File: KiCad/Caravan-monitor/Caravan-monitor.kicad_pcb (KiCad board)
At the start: 2 copper layers, 102.5 x 80 mm, 62 parts, among them IC1 TPS54302DDCR, IC3 INA500CIDBVR, J1 Conn_ARM_JTAG_SWD_20, J2 8-28V input, J3 Outdoor temp, J4 Coolant temp, J5 Water tank 1, J6 Water tank 2, Q1 2N7002, SW2 SW_USER, SW3 SW_DPDT_x2, U1 NHD-C0220BIZ, U2 STM32L010C6Tx

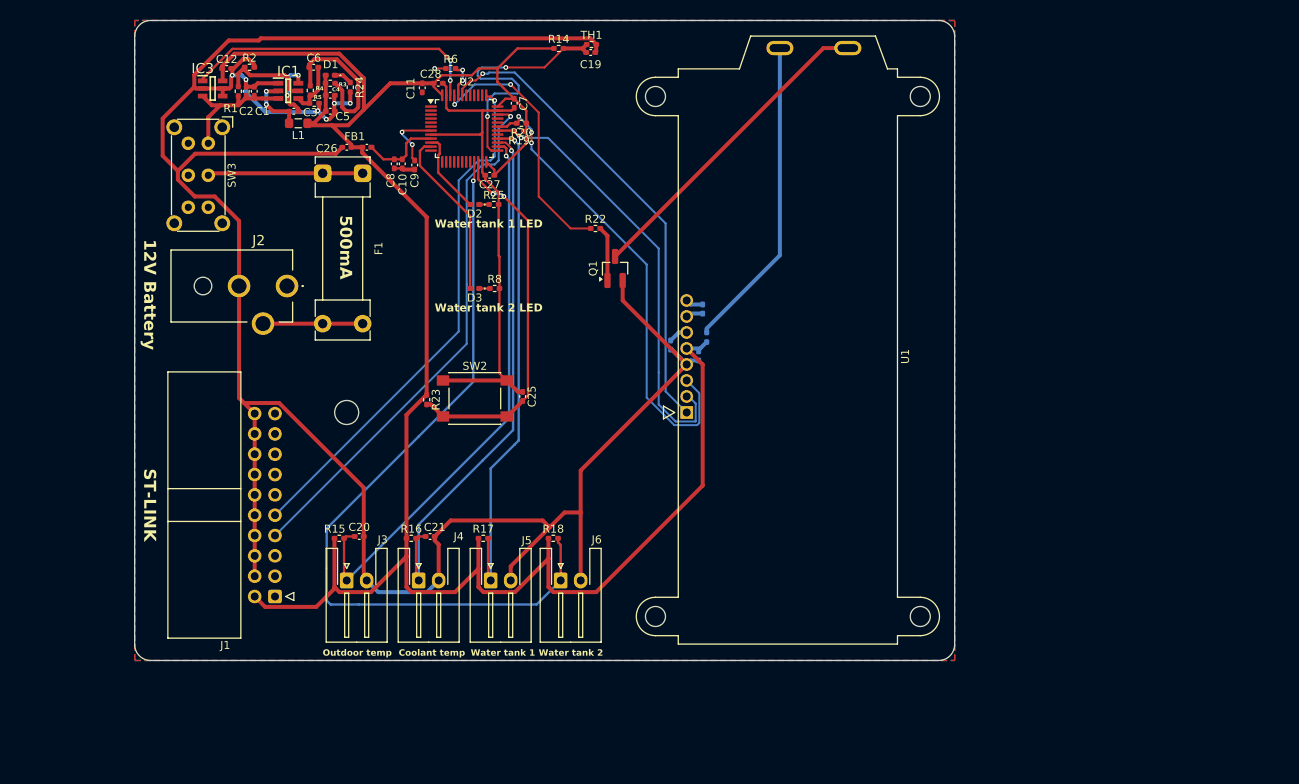
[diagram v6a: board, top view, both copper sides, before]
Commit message: 12V to 3.3V converter done
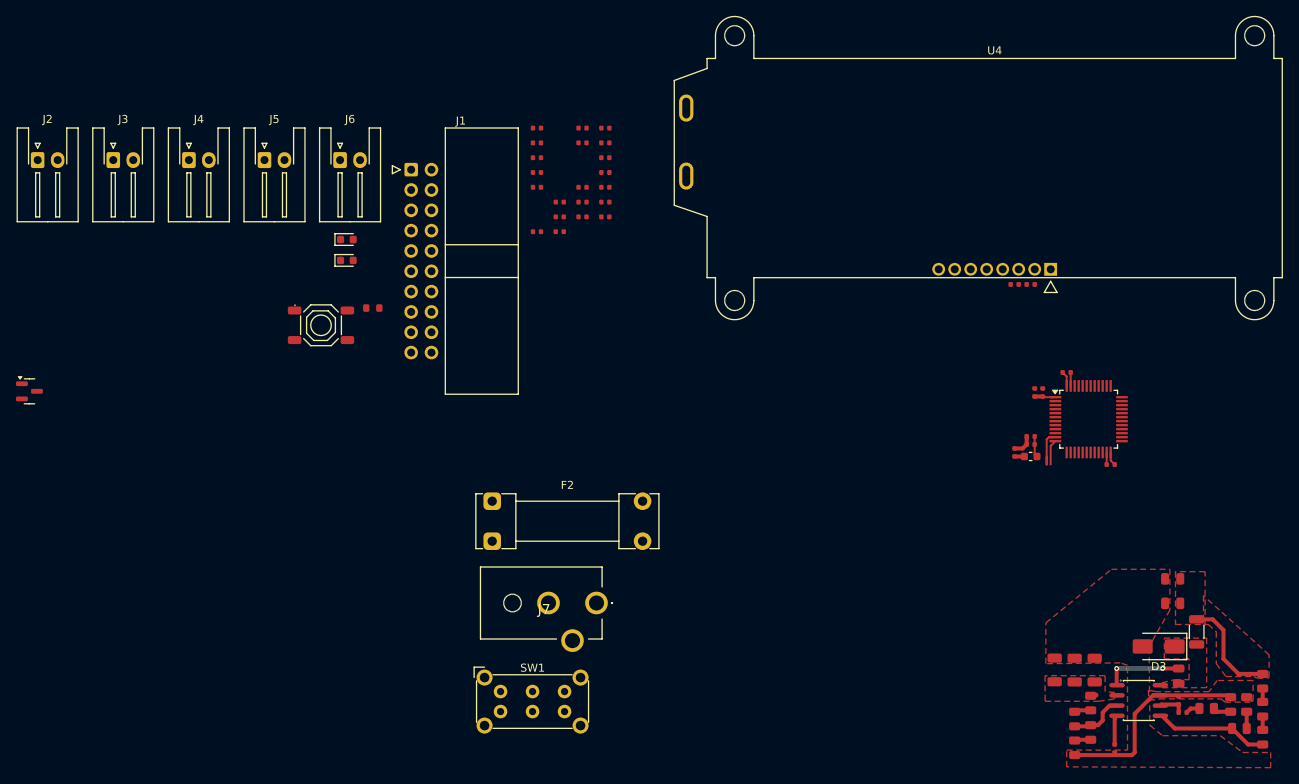
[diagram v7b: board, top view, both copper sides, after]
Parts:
- removed C19, C20, C22, C25, C27, C28: 100n, Capacitor_SMD:C_0402_1005Metric_Pad0.74x0.62mm_HandSolder
- removed C23: 0.47µ, Capacitor_SMD:C_0402_1005Metric_Pad0.74x0.62mm_HandSolder
- removed C26: 1µ, Capacitor_SMD:C_0402_1005Metric_Pad0.74x0.62mm_HandSolder
- removed D1: Power LED, LED_SMD:LED_0402_1005Metric_Pad0.77x0.64mm_HandSolder
- removed F1: 500mA, Fuse:Fuseholder_Clip-5x20mm_Littelfuse_111_Lateral_P18.80x5.00mm_D1.17mm_Horizontal
- removed G***: LOGO, LOGO
- removed IC1: TPS54302DDCR, SamacSys_Parts:SOT95P280X110-6N
- removed IC3: INA500CIDBVR, SamacSys_Parts:SOT95P280X145-6N
- removed L1: 6.8µ, Inductor_SMD:L_0805_2012Metric_Pad1.05x1.20mm_HandSolder
- removed R14: 47k, Resistor_SMD:R_0402_1005Metric_Pad0.72x0.64mm_HandSolder
- removed R17, R23: 10k, Resistor_SMD:R_0402_1005Metric_Pad0.72x0.64mm_HandSolder
- removed R20: 4.7k, Resistor_SMD:R_0402_1005Metric_Pad0.72x0.64mm_HandSolder
- removed R21: 10R, Resistor_SMD:R_0402_1005Metric_Pad0.72x0.64mm_HandSolder
- removed R22, R24, R25: 1k, Resistor_SMD:R_0402_1005Metric_Pad0.72x0.64mm_HandSolder
- removed SW2: SW_USER, Button_Switch_SMD:SW_SPST_PTS645
- removed SW3: SW_DPDT_x2, Button_Switch_THT:SW_E-Switch_EG2219_DPDT_Angled
- removed TH1: Thermistor_NTC, Resistor_SMD:R_0402_1005Metric_Pad0.72x0.64mm_HandSolder
- removed U1: NHD-C0220BIZ, Display:NHD-C0220BiZ
- added C13: 100nF, PCM_JLCPCB:C_0402, F.Cu at (147.5, 88.0)
- added C14: 10nF, PCM_JLCPCB:C_0402, F.Cu at (146.0, 93.5)
- added C15: 100nF, PCM_JLCPCB:C_0402, F.Cu at (87.1, 64.2)
- added C16: 100nF, PCM_JLCPCB:C_0402, F.Cu at (87.1, 66.0)
- added C17: 4.7uF, PCM_JLCPCB:C_1206, F.Cu at (151.5, 122.7)
- added C18: 10nF, PCM_JLCPCB:C_1206, F.Cu at (149.0, 122.7)
- added C30: 1nF, PCM_JLCPCB:C_0402, F.Cu at (165.0, 128.0)
- added C31: 47pF, PCM_JLCPCB:C_0402, F.Cu at (164.5, 126.5)
- added C32: 100nF, PCM_JLCPCB:C_0805, F.Cu at (164.5, 123.5)
- added C33: 47uF, PCM_JLCPCB:C_0805, F.Cu at (163.8, 114.3)
- added C34: 47uF, PCM_JLCPCB:C_0805, F.Cu at (163.8, 111.3)
- added D5: Red, PCM_JLCPCB:D_0603, F.Cu at (60.5, 71.5)
- added F2: 500mA, Fuse:Fuseholder_Clip-5x20mm_Littelfuse_111_Lateral_P18.80x5.00mm_D1.17mm_Horizontal, F.Cu at (78.7, 101.6)
- added J7: 12V DC jack, SamacSys_Parts:PJ059A, F.Cu at (91.7, 114.3)
- added L2: 10uH,25mA, PCM_JLCPCB:L_1206, F.Cu at (166.8, 117.9)
- added R10: 47kΩ, PCM_JLCPCB:R_0402, F.Cu at (92.8, 55.0)
- added R11: 47kΩ, PCM_JLCPCB:R_0402, F.Cu at (92.8, 56.8)
- added R13: 10kΩ, PCM_JLCPCB:R_0402, F.Cu at (92.8, 58.6)
- added R28: 330kΩ, PCM_JLCPCB:R_0805, F.Cu at (151.5, 128.8)
- added R29: 68kΩ, PCM_JLCPCB:R_0805, F.Cu at (153.5, 130.5)
- added R30: 100Ω, PCM_JLCPCB:R_0805, F.Cu at (151.5, 132.4)
- added R31: 27kΩ, PCM_JLCPCB:R_0805, F.Cu at (168.0, 127.5)
- added R32: 2.4kΩ, PCM_JLCPCB:R_0805, F.Cu at (171.0, 127.0)
- added R33: 0Ω, PCM_JLCPCB:R_0805, F.Cu at (175.0, 124.1)
- added R34: 10kΩ, PCM_JLCPCB:R_0805, F.Cu at (175.0, 127.6)
- added R35: 200Ω, PCM_JLCPCB:R_0805, F.Cu at (175.0, 131.1)
- added R36: 240Ω, PCM_JLCPCB:R_0805, F.Cu at (172.1, 130.0)
- added R37: 3kΩ, PCM_JLCPCB:R_0805, F.Cu at (173.0, 127.0)
- added R7: 10kΩ, PCM_JLCPCB:R_0402, F.Cu at (90.0, 66.0)
- added R9: 10Ω, PCM_JLCPCB:R_0603, F.Cu at (63.8, 77.5)
- added S1: Tactile Button, 160gf, PCM_JLCPCB:SW-SMD_4P-L5.1-W5.1-P3.70-LS6.5-TL-2, F.Cu at (57.3, 79.6)
- added SW1: SW_DPDT_x2, Button_Switch_THT:SW_E-Switch_EG2219_DPDT_Angled, F.Cu at (79.7, 125.4)
- added U3: TPS54331DR, PCM_JLCPCB:SOIC-8_L5.0-W4.0-P1.27-LS6.0-BL, F.Cu at (159.5, 126.5)
- added U4: NHD-C0220BIZ, Display:NHD-C0220BiZ, F.Cu at (141.5, 56.7)
- C1: value 0.1µ -> 470nF; footprint Capacitor_SMD:C_0402_1005Metric_Pad0.74x0.62mm_HandSolder -> PCM_JLCPCB:C_0402
- C10, C11: value 1µ -> 1uF; footprint Capacitor_SMD:C_0402_1005Metric_Pad0.74x0.62mm_HandSolder -> PCM_JLCPCB:C_0402
- C12: value 100n -> 4.7uF; footprint Capacitor_SMD:C_0402_1005Metric_Pad0.74x0.62mm_HandSolder -> PCM_JLCPCB:C_1206
- C2: value 10µ -> 100nF; footprint Capacitor_SMD:C_0402_1005Metric_Pad0.74x0.62mm_HandSolder -> PCM_JLCPCB:C_0402
- C21, C9: value 100n -> 100nF; footprint Capacitor_SMD:C_0402_1005Metric_Pad0.74x0.62mm_HandSolder -> PCM_JLCPCB:C_0402
- C24: value 100n -> 10nF; footprint Capacitor_SMD:C_0402_1005Metric_Pad0.74x0.62mm_HandSolder -> PCM_JLCPCB:C_0402; moved to F.Cu
- C3: value 0.1µ -> 100nF; footprint Capacitor_SMD:C_0402_1005Metric_Pad0.74x0.62mm_HandSolder -> PCM_JLCPCB:C_0402
- C4, C5: value 22µ -> 100nF; footprint Capacitor_SMD:C_0402_1005Metric_Pad0.74x0.62mm_HandSolder -> PCM_JLCPCB:C_0402
- C6: value 47p -> 100nF; footprint Capacitor_SMD:C_0402_1005Metric_Pad0.74x0.62mm_HandSolder -> PCM_JLCPCB:C_0402
- C7: value 100n -> 1uF; footprint Capacitor_SMD:C_0402_1005Metric_Pad0.74x0.62mm_HandSolder -> PCM_JLCPCB:C_0402
- C8: value 10n -> 100nF; footprint Capacitor_SMD:C_0402_1005Metric_Pad0.74x0.62mm_HandSolder -> PCM_JLCPCB:C_0402
- D2: value WT1_LED -> Red; footprint LED_SMD:LED_0402_1005Metric_Pad0.77x0.64mm_HandSolder -> PCM_JLCPCB:D_0603
- D3: value WT2_LED -> SS34; footprint LED_SMD:LED_0402_1005Metric_Pad0.77x0.64mm_HandSolder -> Diode_SMD:D_SMA
- FB1: value 120R -> ~; footprint Inductor_SMD:L_0402_1005Metric_Pad0.77x0.64mm_HandSolder -> PCM_JLCPCB:FB_0603
- J2: value 8-28V input -> Water tank 2; footprint SamacSys_Parts:PJ059A -> Connector_JST:JST_XH_S2B-XH-A-1_1x02_P2.50mm_Horizontal
- J3: value Outdoor temp -> Indoor temp
- J4: value Coolant temp -> Outdoor temp
- J6: value Water tank 2 -> Coolant temp
- Q1: footprint Package_TO_SOT_SMD:SOT-23_Handsoldering -> PCM_JLCPCB:Q_SOT-23
- R1: value 511k -> 1kΩ; footprint Resistor_SMD:R_0402_1005Metric_Pad0.72x0.64mm_HandSolder -> PCM_JLCPCB:R_0402
- R15: value 47k -> 10kΩ; footprint Resistor_SMD:R_0402_1005Metric_Pad0.72x0.64mm_HandSolder -> PCM_JLCPCB:R_0402
- R16: value 10k -> 10kΩ; footprint Resistor_SMD:R_0402_1005Metric_Pad0.72x0.64mm_HandSolder -> PCM_JLCPCB:R_0402
- R18: value 10k -> 100kΩ; footprint Resistor_SMD:R_0402_1005Metric_Pad0.72x0.64mm_HandSolder -> PCM_JLCPCB:R_0402
- R19: value 4.7k -> 27kΩ; footprint Resistor_SMD:R_0402_1005Metric_Pad0.72x0.64mm_HandSolder -> PCM_JLCPCB:R_0402
- R2: value 105k -> 10kΩ; footprint Resistor_SMD:R_0402_1005Metric_Pad0.72x0.64mm_HandSolder -> PCM_JLCPCB:R_0402
- R3: value 49.9 -> 4.7kΩ; footprint Resistor_SMD:R_0402_1005Metric_Pad0.72x0.64mm_HandSolder -> PCM_JLCPCB:R_0402
- R4: value 100k -> 4.7kΩ; footprint Resistor_SMD:R_0402_1005Metric_Pad0.72x0.64mm_HandSolder -> PCM_JLCPCB:R_0402
- R5: value 22.1k -> 1kΩ; footprint Resistor_SMD:R_0402_1005Metric_Pad0.72x0.64mm_HandSolder -> PCM_JLCPCB:R_0402
- R6: value 10k -> 1kΩ; footprint Resistor_SMD:R_0402_1005Metric_Pad0.72x0.64mm_HandSolder -> PCM_JLCPCB:R_0402
- R8: value 1k -> 2kΩ; footprint Resistor_SMD:R_0402_1005Metric_Pad0.72x0.64mm_HandSolder -> PCM_JLCPCB:R_0805
- U2: value STM32L010C6Tx -> STM32F030C8T6; footprint Package_QFP:LQFP-48_7x7mm_P0.5mm -> PCM_JLCPCB:LQFP-48_7x7mm_P0.5mm
- moved C12 132.0 mm to (154.0, 122.7), turned to 90 degrees
- moved C6 111.3 mm to (156.0, 97.0), turned to 180 degrees
- moved D3 96.5 mm to (162.0, 119.8)
- moved FB1 91.5 mm to (146.0, 96.0)
- moved R4 91.3 mm to (144.0, 74.5), turned to 0 degrees
- moved R3 91.1 mm to (146.0, 74.5)
- moved R8 90.7 mm to (153.5, 126.8), turned to -90 degrees
- moved C11 87.0 mm to (144.0, 95.5), turned to 90 degrees
- moved U2 86.1 mm to (153.2, 91.3)
- moved C10 86.0 mm to (146.0, 94.5), turned to 180 degrees
- moved C9 85.5 mm to (150.5, 85.5), turned to 0 degrees
- moved Q1 74.8 mm to (20.8, 87.9), turned to 0 degrees
- moved C7 74.4 mm to (146.5, 88.0), turned to 90 degrees
- moved C24 71.5 mm to (156.5, 132.5)
- moved J3 60.1 mm to (31.3, 59.0)
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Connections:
- C1 pad 1: +BATT -> Net-(U4-VOUT)
- C12 pad 1: +3.3V -> +12V
- C2 pad 1: +BATT -> +3.3V
- C21 pad 1: CoolantTemp -> BatteryVoltage
- C24 pad 1: +3.3V -> Net-(U3-SS)
- C4 pad 1: +3.3V -> CoolantTemp
- C5 pad 1: +3.3V -> /NRST
- C6 pad 1: Net-(C6-Pad1) -> +3.3V
- C6 pad 2: Net-(IC1-FB) -> GND
- C8 pad 1: +3.3VA -> Net-(S1-A)
- C9 pad 1: GND -> +3.3V
- C9 pad 2: /NRST -> GND
- D2 pad 1: Net-(D2-K) -> Net-(D2-Pad1)
- D2 pad 2: Net-(D2-A) -> /WaterTank2LED
- D3 pad 1: Net-(D3-K) -> /PowerSupply/PH
- D3 pad 2: Net-(D3-A) -> GND
- J2 pad 1: unconnected-(J2-Pad1) -> WaterTank2
- J3 pad 1: OutdoorTemp -> IndoorTemp
- J4 pad 1: CoolantTemp -> OutdoorTemp
- J5 pad 1: WaterTank1 -> GND
- J5 pad 2: GND -> WaterTank1
- J6 pad 1: WaterTank2 -> CoolantTemp
- Q1 pad 3: /Display/BL_Cathode -> /BL_Cathode
- R1 pad 1: +BATT -> DisplayBacklight
- R1 pad 2: Net-(IC1-EN) -> Net-(Q1-G)
- R15 pad 2: OutdoorTemp -> CoolantTemp
- R16 pad 2: CoolantTemp -> WaterTank2
- R18 pad 1: +3.3V -> +12V
- R18 pad 2: WaterTank2 -> BatteryVoltage
- R19 pad 1: +3.3V -> BatteryVoltage
- R19 pad 2: SCL -> GND
- R2 pad 1: Net-(IC1-EN) -> /BOOT0
- R3 pad 2: Net-(C6-Pad1) -> SCL
- R4 pad 1: Net-(C6-Pad1) -> +3.3V
- R4 pad 2: Net-(IC1-FB) -> SDA
- R5 pad 1: Net-(IC1-FB) -> Net-(D2-Pad1)
- R6 pad 1: GND -> Net-(D5-Pad1)
- R6 pad 2: /BOOT0 -> GND
- R8 pad 1: Net-(D3-K) -> +12V
- R8 pad 2: GND -> Net-(R28-Pad1)
- U2 pad 1: unconnected-(U2-PC0-Pad1) -> +3.3V
- U2 pad 10: Net-(D2-A) -> unconnected-(U2-PA0-Pad10)
- U2 pad 11: Net-(D3-A) -> IndoorTemp
- U2 pad 12: unconnected-(U2-PA2-Pad12) -> OutdoorTemp
- U2 pad 13: unconnected-(U2-PA3-Pad13) -> CoolantTemp
- U2 pad 14: unconnected-(U2-PA4-Pad14) -> WaterTank1
- U2 pad 15: unconnected-(U2-PA5-Pad15) -> WaterTank2
- U2 pad 16: unconnected-(U2-PA6-Pad16) -> BatteryVoltage
- U2 pad 21: WaterTank2 -> unconnected-(U2-PB10-Pad21)
- U2 pad 22: Net-(SW2-B) -> Net-(S1-A)
- U2 pad 25: IndoorTemp -> unconnected-(U2-PB12-Pad25)
- U2 pad 26: OutdoorTemp -> unconnected-(U2-PB13-Pad26)
- U2 pad 27: CoolantTemp -> unconnected-(U2-PB14-Pad27)
- U2 pad 28: WaterTank1 -> unconnected-(U2-PB15-Pad28)
- U2 pad 29: unconnected-(U2-PA8-Pad29) -> /WaterTank1LED
- U2 pad 30: SCL -> /WaterTank2LED
- U2 pad 31: SDA -> unconnected-(U2-PA10-Pad31)
- U2 pad 35: GND -> unconnected-(U2-PF6-Pad35)
- U2 pad 36: +3.3V -> unconnected-(U2-PF7-Pad36)
- U2 pad 40: unconnected-(U2-PB4-Pad40) -> DisplayReset
- U2 pad 41: unconnected-(U2-PB5-Pad41) -> DisplayBacklight
- U2 pad 42: unconnected-(U2-PB6-Pad42) -> SCL
- U2 pad 43: DisplayReset -> SDA
- U2 pad 45: DisplayBacklight -> unconnected-(U2-PB8-Pad45)
- U2 pad 46: BatteryVoltage -> unconnected-(U2-PB9-Pad46)
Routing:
- net GND: track 381.1 -> 31.5 mm, vias 7 -> 0
- net +3.3V: track 263.4 -> 20.6 mm
- net WaterTank2: track 98.6 -> 0.00 mm, vias 1 -> 0
- net CoolantTemp: track 67.7 -> 0.00 mm, vias 1 -> 0
- net OutdoorTemp: track 70.6 -> 3.15 mm, vias 1 -> 0
- net SWDIO: track 67.2 -> 0.00 mm, vias 1 -> 0
- net SWCLK: track 65.4 -> 0.00 mm, vias 1 -> 0
- net WaterTank1: track 64.3 -> 0.00 mm, vias 1 -> 0
- net DisplayReset: track 59.6 -> 0.00 mm, vias 1 -> 0
- net SDA: track 59.4 -> 0.00 mm, vias 3 -> 0
- net SCL: track 55.0 -> 0.00 mm, vias 1 -> 0
- net Net-(SW2-B): track 46.8 -> 0.00 mm, vias 2 -> 0
- net /Display/BL_Cathode: track 39.9 -> 0.00 mm
- net /Display/BL_Anode: track 39.3 -> 0.00 mm
- net BatteryVoltage: track 37.8 -> 0.00 mm, vias 2 -> 0
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- added copper zone on F.Cu, net +12V
- added copper zone on F.Cu, net +3.3V
- added copper zone on F.Cu, net /PowerSupply/PH
- removed copper zone on B.Cu, net GND
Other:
- board outline removed
- board text removed: "12V Battery"
- board text removed: "500mA"
- board text removed: "Coolant temp"
- board text removed: "Outdoor temp"
- board text removed: "ST-LINK"
- board text removed: "V0.1 5/26"
- board text removed: "Water tank 1"
- board text removed: "Water tank 1 LED"
- board text removed: "Water tank 2"
- board text removed: "Water tank 2 LED"
- board text removed: "https://github.com/peltonenmikko/Caravan-Monitor"

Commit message: V0.2 PCB complete
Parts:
- removed C3: 100nF, PCM_JLCPCB:C_0402
- removed F2: 500mA, Fuse:Fuseholder_Clip-5x20mm_Littelfuse_111_Lateral_P18.80x5.00mm_D1.17mm_Horizontal
- removed J1: Conn_ARM_JTAG_SWD_20, Connector_IDC:IDC-Header_2x10_P2.54mm_Horizontal
- removed J2: Water tank 2, Connector_JST:JST_XH_S2B-XH-A-1_1x02_P2.50mm_Horizontal
- removed J3: Indoor temp, Connector_JST:JST_XH_S2B-XH-A-1_1x02_P2.50mm_Horizontal
- removed J4: Outdoor temp, Connector_JST:JST_XH_S2B-XH-A-1_1x02_P2.50mm_Horizontal
- removed J5: Water tank 1, Connector_JST:JST_XH_S2B-XH-A-1_1x02_P2.50mm_Horizontal
- removed J6: Coolant temp, Connector_JST:JST_XH_S2B-XH-A-1_1x02_P2.50mm_Horizontal
- removed J7: 12V DC jack, SamacSys_Parts:PJ059A
- removed L2: 10uH,25mA, PCM_JLCPCB:L_1206
- removed Q1: 2N7002, PCM_JLCPCB:Q_SOT-23
- removed R1: 1kΩ, PCM_JLCPCB:R_0402
- removed R9: 10Ω, PCM_JLCPCB:R_0603
- removed SW1: SW_DPDT_x2, Button_Switch_THT:SW_E-Switch_EG2219_DPDT_Angled
- added C19: 12pF, PCM_JLCPCB:C_0402, F.Cu at (173.2, 104.0)
- added C20: 12pF, PCM_JLCPCB:C_0402, F.Cu at (173.1, 109.0)
- added CN2: HX JN1.27-2X7P ZZ H4.9, EasyEDA:IDC-TH_14P-P1.27_C42455940, F.Cu at (193.7, 99.6)
- added D1: Red, PCM_JLCPCB:D_0805, F.Cu at (163.8, 108.7)
- added DC1: DC-005-A250, EasyEDA:DC-IN-TH_DC-005-A250, F.Cu at (199.5, 131.7)
- added FH1: 64600001003, EasyEDA:64600001003, F.Cu at (189.5, 122.7)
- added L1: FXL0630-6R8-M, EasyEDA:IND-SMD_L7.0-W6.6, F.Cu at (169.4, 118.9)
- added R12: 0Ω, PCM_JLCPCB:R_0402, F.Cu at (175.3, 108.4)
- added R14: 1kΩ, PCM_JLCPCB:R_0402, F.Cu at (161.4, 109.8)
- added S2: Tactile Button, 160gf, PCM_JLCPCB:SW-SMD_4P-L5.1-W5.1-P3.70-LS6.5-TL-2, F.Cu at (193.4, 80.8)
- added U1: S2B-PH-K-S, EasyEDA:CONN-TH_S2B-PH-K-S-LF-SN, F.Cu at (151.5, 107.3)
- added U5: S2B-PH-K-S, EasyEDA:CONN-TH_S2B-PH-K-S-LF-SN, F.Cu at (151.5, 100.1)
- added U6: S2B-PH-K-S, EasyEDA:CONN-TH_S2B-PH-K-S-LF-SN, F.Cu at (151.5, 92.8)
- added U7: S2B-PH-K-S, EasyEDA:CONN-TH_S2B-PH-K-S-LF-SN, F.Cu at (151.5, 85.6)
- added U8: S2B-PH-K-S, EasyEDA:CONN-TH_S2B-PH-K-S-LF-SN, F.Cu at (151.4, 78.3)
- added U9: SS-12M12G5, EasyEDA:SW-TH_SS-12M12G5, F.Cu at (183.4, 131.3)
- added X1: X322516MLB4SI, PCM_JLCPCB:OSC-SMD_4P-L3.2-W2.5-BL, F.Cu at (173.2, 106.5)
- C1: value 470nF -> 100nF
- U4: value NHD-C0220BIZ -> HS96L03W2C03; footprint Display:NHD-C0220BiZ -> EasyEDA:OLED-TH_L27.8-W27.2-P2.54_C9900033791
- moved D2 127.2 mm to (184.7, 96.8), turned to 180 degrees
- moved D5 124.9 mm to (184.7, 85.1), turned to 180 degrees
- moved C1 114.1 mm to (180.6, 116.1)
- moved C5 113.9 mm to (196.7, 80.9), turned to 90 degrees
- moved S1 112.9 mm to (168.1, 101.1), turned to -90 degrees
- moved C2 111.4 mm to (178.6, 116.1), turned to 180 degrees
- moved C8 109.6 mm to (183.3, 114.8)
- moved C4 108.5 mm to (178.0, 115.1), turned to 180 degrees
- moved C21 104.7 mm to (181.1, 114.0)
- moved R5 103.4 mm to (187.5, 96.8)
- moved C16 102.2 mm to (177.3, 114.2)
- moved C15 101.4 mm to (175.4, 114.2), turned to 180 degrees
- moved R2 100.9 mm to (180.3, 101.9), turned to 90 degrees
- moved R6 99.7 mm to (187.4, 85.1)
- moved R7 87.2 mm to (168.3, 104.4)
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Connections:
- net /NRST renamed NRST
- C1 pad 1: Net-(U4-VOUT) -> WaterTank2
- C2 pad 1: +3.3V -> WaterTank1
- U2 pad 40: DisplayReset -> unconnected-(U2-PB4-Pad40)
- U2 pad 41: DisplayBacklight -> unconnected-(U2-PB5-Pad41)
- U2 pad 5: unconnected-(U2-PF0-Pad5) -> Net-(U2-PF0)
- U2 pad 6: unconnected-(U2-PF1-Pad6) -> Net-(U2-PF1)
- U4 pad 1: DisplayReset -> GND
- U4 pad 2: SCL -> +3.3V
- U4 pad 3: SDA -> SCL
- U4 pad 4: GND -> SDA
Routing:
- net +3.3V: track 20.6 -> 193.8 mm
- net GND: track 31.5 -> 143.7 mm, vias 0 -> 27
- net BatteryVoltage: track 0.00 -> 60.3 mm, vias 0 -> 4
- net OutdoorTemp: track 3.15 -> 59.3 mm, vias 0 -> 4
- net SCL: track 0.00 -> 53.0 mm, vias 0 -> 2
- net NRST: track 0.00 -> 51.1 mm, vias 0 -> 2
- net CoolantTemp: track 0.00 -> 47.7 mm, vias 0 -> 4
- net IndoorTemp: track 5.34 -> 52.9 mm, vias 0 -> 4
- net Net-(S1-A): track 0.00 -> 46.3 mm, vias 0 -> 6
- net WaterTank2: track 0.00 -> 45.2 mm, vias 0 -> 4
- net WaterTank1: track 0.00 -> 40.1 mm, vias 0 -> 4
- net SDA: track 0.00 -> 36.1 mm
- net /WaterTank1LED: track 0.00 -> 30.0 mm, vias 0 -> 2
- net /WaterTank2LED: track 0.00 -> 14.9 mm, vias 0 -> 2
- net +12V: track 0.83 -> 13.0 mm
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- added copper zone on F.Cu, net /PowerSupply/Battery 12V
- added copper zone on F.Cu, net /PowerSupply/Battery 12V fused
- added copper zone on B.Cu, net GND
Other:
- board outline added: 61.2 x 73.4 mm
- board text added: "12V"
- board text added: "3.3V"
- board text added: "500mA Time-Lag"
- board text added: "Coolant temp"
- board text added: "GND"
- board text added: "Indoor temp"
- board text added: "NC"
- board text added: "NRST"
- board text added: "Outdoor temp"
- board text added: "Power LED"
- board text added: "RESET"
- board text added: "SWCLK"
- board text added: "SWD STDC14"
- board text added: "SWDIO"
- board text added: "USER"
- board text added: "V0.2"
- board text added: "WT1_LED"
- board text added: "WT2_LED"
- board text added: "Water tank 1"
- board text added: "Water tank 2"
- board text added: "https://github.com/peltonenmikko/Caravan-Monitor"
